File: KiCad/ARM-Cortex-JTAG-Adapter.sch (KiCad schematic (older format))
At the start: 5 parts, among them J1 Data, J2 Power

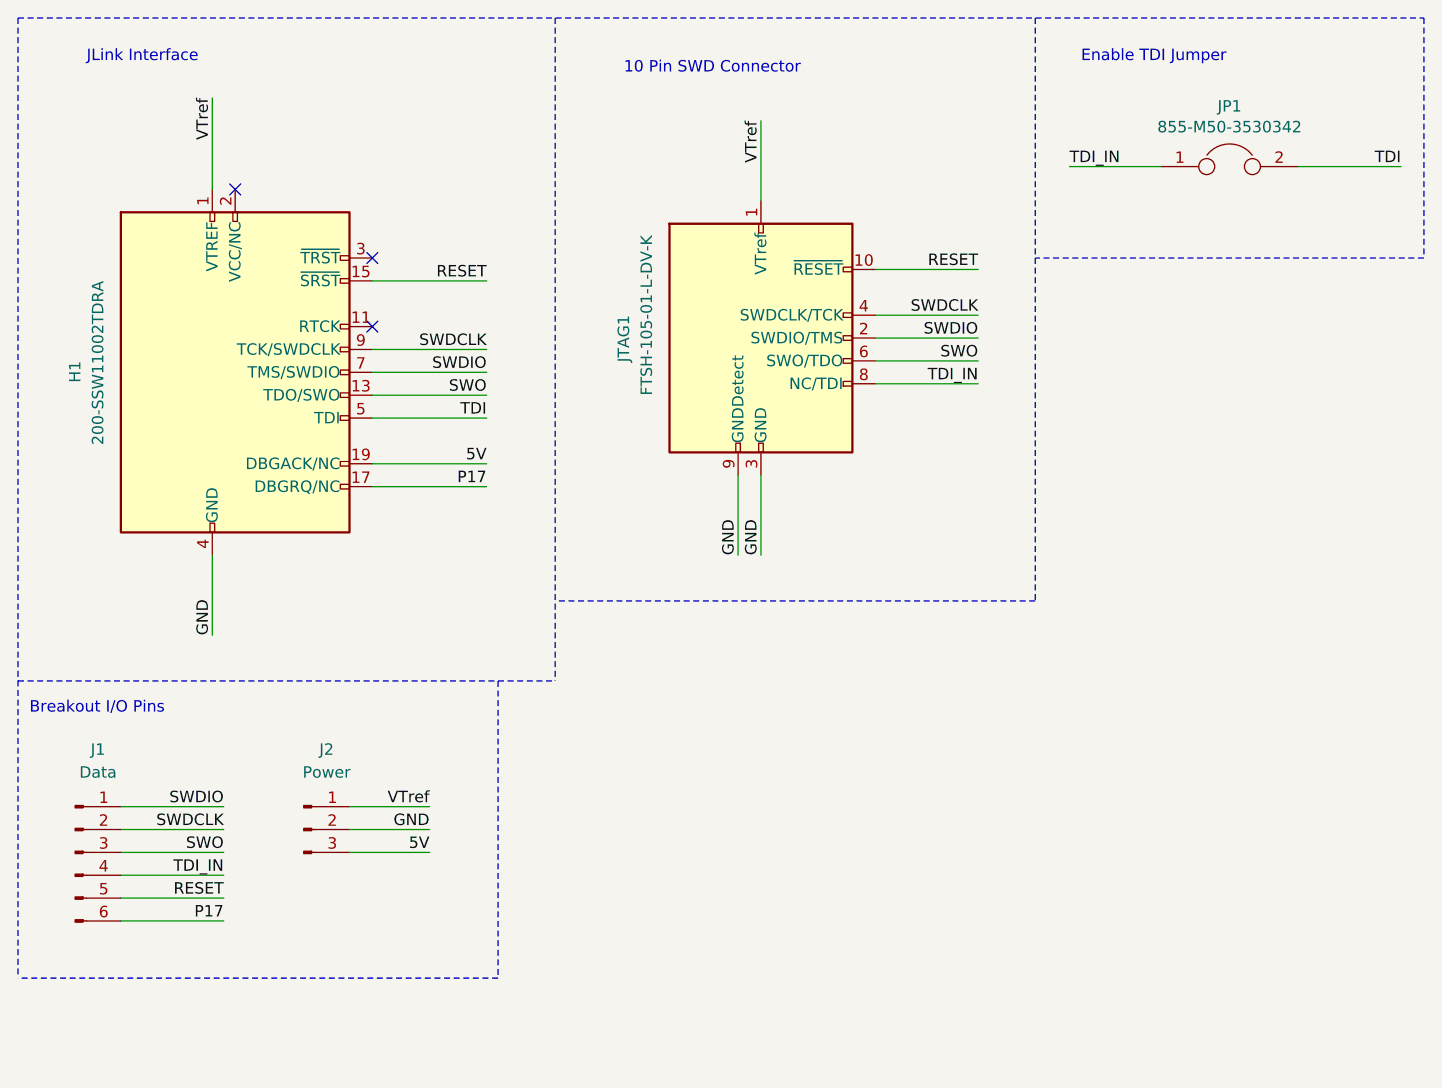
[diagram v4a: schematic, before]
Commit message: Redoing footprints and symbols.
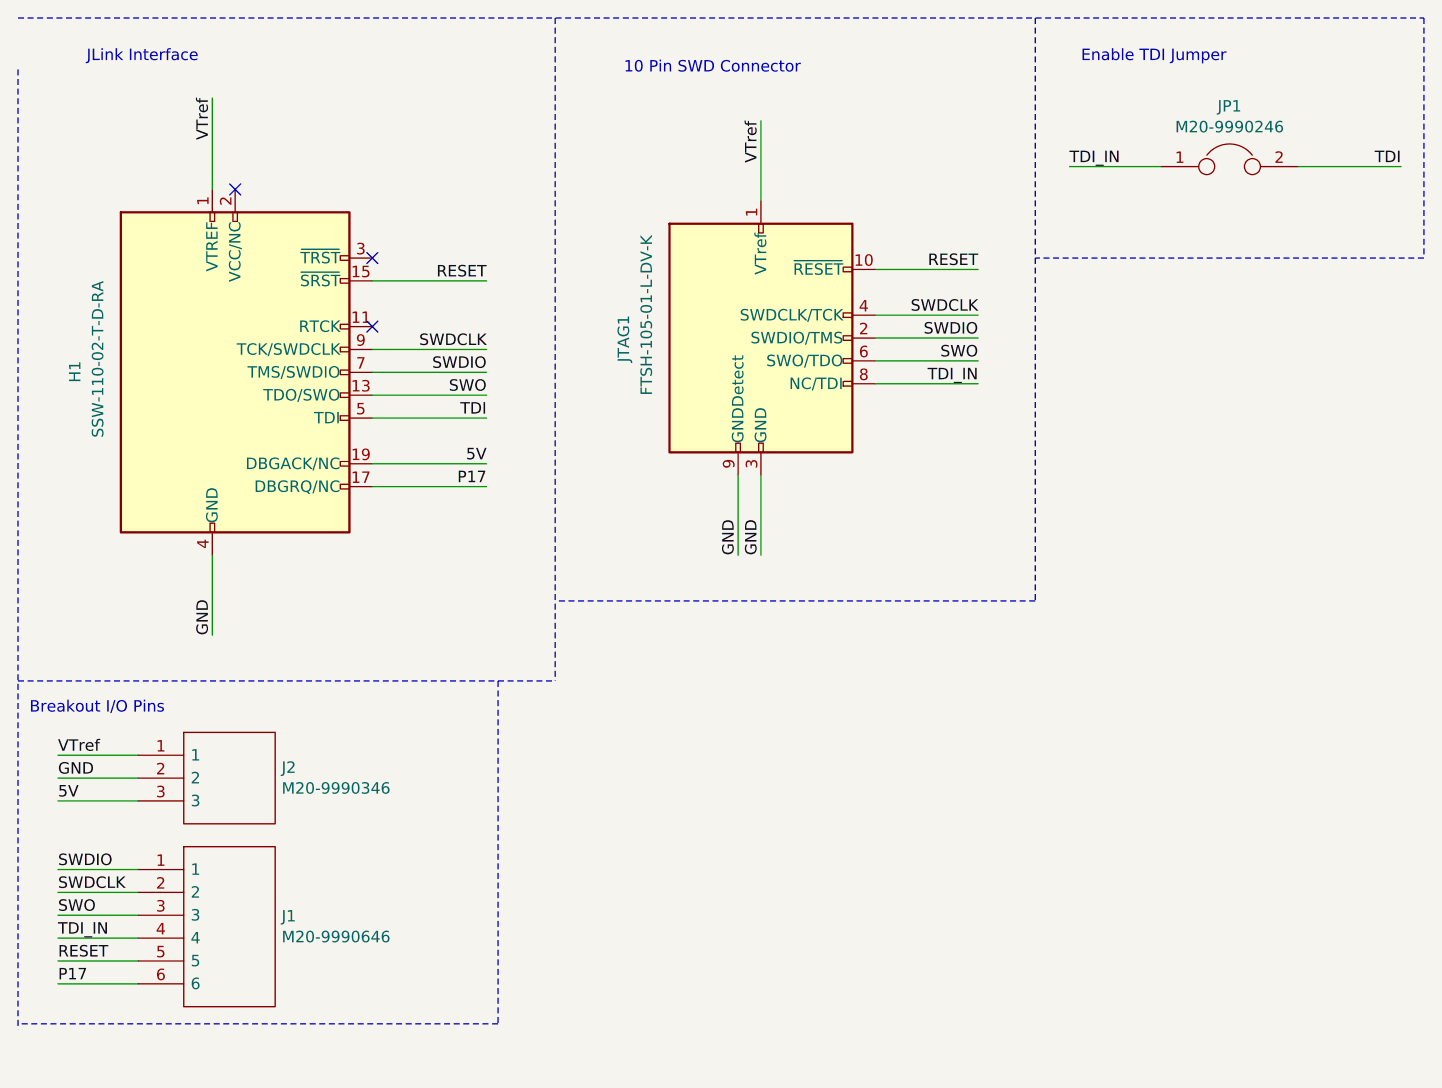
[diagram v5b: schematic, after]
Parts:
- removed J1: Data, Connector_PinHeader_2.54mm:PinHeader_1x06_P2.54mm_Vertical, symbol Connector:Conn_01x06_Male
- removed J2: Power, Connector_PinHeader_2.54mm:PinHeader_1x03_P2.54mm_Vertical, symbol Connector:Conn_01x03_Male
- added J1: M20-9990646, (Local):m20-9990646, symbol m20-9990646:M20-9990646
- added J2: M20-9990346, (Local):m20-9990346, symbol m20-9990346:M20-9990346
- H1: value 200-SSW11002TDRA -> SSW-110-02-T-D-RA
- JP1: value 855-M50-3530342 -> M20-9990246; footprint Connector_PinHeader_2.54mm:PinHeader_1x02_P2.54mm_Vertical -> (Local):M20-9990246
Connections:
- net 5V: now also J2.3
- net GND: now also J2.2
- net P17: now also J1.6
- net RESET: now also J1.5
- net SWDCLK: now also J1.2
- net SWDIO: now also J1.1
- net SWO: now also J1.3
- net TDI_IN: now also J1.4
- net VTref: now also J2.1
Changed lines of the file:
@@
 RESET
-$Comp
-L Connector:Conn_01x03_Male J2
-U 1 1 5F65A72D
-P 2450 4300
-F 0 "J2" H 2550 4650 50  0000 C CNN
-F 1 "Power" H 2550 4550 50  0000 C CNN
-F 2 "Connector_PinHeader_2.54mm:PinHeader_1x03_P2.54mm_Vertical" H 2450 4300 50  0001 C CNN
-F 3 "~" H 2450 4300 50  0001 C CNN
-	1    2450 4300
-	1    0    0    -1
-$EndComp
-Wire Wire Line
-	2650 4200 3000 4200
-Text Label 3000 4400 2    50   ~ 0
-5V
-Wire Wire Line
-	2650 4300 3000 4300
-Text Label 3000 4300 2    50   ~ 0
-GND
-Wire Wire Line
-	2650 4400 3000 4400
-Text Label 3000 4200 2    50   ~ 0
-VTref
-Wire Wire Line
-	1650 4200 2100 4200
-Text Label 2100 4300 2    50   ~ 0
-SWDCLK
-Wire Wire Line
-	1650 4300 2100 4300
-Text Label 2100 4200 2    50   ~ 0
-SWDIO
-Wire Wire Line
-	1650 4400 2100 4400
-Text Label 2100 4400 2    50   ~ 0
-SWO
-Wire Wire Line
-	1650 4500 2100 4500
-Text Label 2100 4500 2    50   ~ 0
-TDI_IN
 $Comp
 L Connector:Conn_ARM_JTAG_SWD_20 H1
@@
 P 2150 2300
 F 0 "H1" V 1450 2350 50  0000 R CNN
-F 1 "200-SSW11002TDRA" V 1550 2700 50  0000 R CNN
+F 1 "SSW-110-02-T-D-RA" V 1550 2700 50  0000 R CNN
 F 2 "Connector_IDC:IDC-Header_2x10_P2.54mm_Horizontal" H 2600 1250 50  0001 L TNN
 F 3 "http://infocenter.arm.com/help/topic/com.arm.doc.dui0499b/DUI0499B_system_design_reference.pdf" V 1800 1050 50  0001 C CNN
@@
 Text Label 3250 2800 2    50   ~ 0
 P17
-Wire Wire Line
-	1650 4600 2100 4600
-Text Label 2100 4600 2    50   ~ 0
-RESET
-Wire Wire Line
-	1650 4700 2100 4700
-Text Label 2100 4700 2    50   ~ 0
-P17
-$Comp
-L Connector:Conn_01x06_Male J1
-U 1 1 5F67F15F
-P 1450 4400
-F 0 "J1" H 1550 4850 50  0000 C CNN
-F 1 "Data" H 1550 4750 50  0000 C CNN
-F 2 "Connector_PinHeader_2.54mm:PinHeader_1x06_P2.54mm_Vertical" H 1450 4400 50  0001 C CNN
-F 3 "~" H 1450 4400 50  0001 C CNN
-	1    1450 4400
-	1    0    0    -1
-$EndComp
 Wire Notes Line
-	3300 3650 3300 4950
+	3300 3650 3300 5150
 Wire Notes Line
-	3300 4950 1200 4950
+	3300 5150 1200 5150
 Text Notes 1250 3800 0    50   ~ 0
 Breakout I/O Pins
@@
 	3550 750  3550 3650
 Wire Notes Line
-	1200 750  1200 4950
+	1200 975  1200 5175
 Wire Notes Line
 	1200 3650 3550 3650
@@
 P 6500 1400
 F 0 "JP1" H 6500 1664 50  0000 C CNN
-F 1 "855-M50-3530342" H 6500 1573 50  0000 C CNN
-F 2 "Connector_PinHeader_2.54mm:PinHeader_1x02_P2.54mm_Vertical" H 6500 1400 50  0001 C CNN
+F 1 "M20-9990246" H 6500 1573 50  0000 C CNN
+F 2 "(Local):M20-9990246" H 6500 1400 50  0001 C CNN
 F 3 "~" H 6500 1400 50  0001 C CNN
 	1    6500 1400
@@
 Text Label 5800 1400 0    50   ~ 0
 TDI_IN
+$Comp
+L m20-9990346:M20-9990346 J2
+U 1 1 5F867894
+P 1725 3975
+F 0 "J2" H 2353 3921 50  0000 L CNN
+F 1 "M20-9990346" H 2353 3830 50  0000 L CNN
+F 2 "(Local):m20-9990346" H 2375 4075 50  0001 L CNN
+F 3 "https://componentsearchengine.com/Datasheets/1/M20-9990346.pdf" H 2375 3975 50  0001 L CNN
+F 4 "03 SIL Vertical Pin Header HARWIN M20 Series, 2.54mm Pitch 3 Way 1 Row Straight PCB Header, Solder Termination, 3A" H 2375 3875 50  0001 L CNN "Description"
+F 5 "8.64" H 2375 3775 50  0001 L CNN "Height"
+F 6 "855-M20-9990346" H 2375 3675 50  0001 L CNN "Mouser Part Number"
+F 7 "https://www.mouser.com/Search/Refine.aspx?Keyword=855-M20-9990346" H 2375 3575 50  0001 L CNN "Mouser Price/Stock"
+F 8 "Harwin" H 2375 3475 50  0001 L CNN "Manufacturer_Name"
+F 9 "M20-9990346" H 2375 3375 50  0001 L CNN "Manufacturer_Part_Number"
+	1    1725 3975
+	1    0    0    -1
+$EndComp
+Wire Wire Line
+	1725 3975 1375 3975
+Wire Wire Line
+	1725 4075 1375 4075
+Text Label 1375 4075 0    50   ~ 0
+GND
+Text Label 1375 3975 0    50   ~ 0
+VTref
+Wire Wire Line
+	1725 4175 1375 4175
+Text Label 1375 4175 0    50   ~ 0
+5V
+$Comp
+L m20-9990646:M20-9990646 J1
+U 1 1 5F8664B1
+P 1725 4475
+F 0 "J1" H 2353 4271 50  0000 L CNN
+F 1 "M20-9990646" H 2353 4180 50  0000 L CNN
+F 2 "(Local):m20-9990646" H 2375 4575 50  0001 L CNN
+F 3 "https://componentsearchengine.com/Datasheets/2/M20-9990646.pdf" H 2375 4475 50  0001 L CNN
+F 4 "06 SIL Vertical Pin Header HARWIN M20 Series, 2.54mm Pitch 6 Way 1 Row Straight PCB Header, Solder Termination, 3A" H 2375 4375 50  0001 L CNN "Description"
+F 5 "8.64" H 2375 4275 50  0001 L CNN "Height"
+F 6 "855-M20-9990646" H 2375 4175 50  0001 L CNN "Mouser Part Number"
+F 7 "https://www.mouser.co.uk/ProductDetail/Harwin/M20-9990646?qs=Jph8NoUxIfXDcWZbabSSiw%3D%3D" H 2375 4075 50  0001 L CNN "Mouser Price/Stock"
+F 8 "Harwin" H 2375 3975 50  0001 L CNN "Manufacturer_Name"
+F 9 "M20-9990646" H 2375 3875 50  0001 L CNN "Manufacturer_Part_Number"
+	1    1725 4475
+	1    0    0    -1
+$EndComp
+Wire Wire Line
+	1725 4475 1375 4475
+Wire Wire Line
+	1725 4575 1375 4575
+Wire Wire Line
+	1725 4675 1375 4675
+Wire Wire Line
+	1725 4775 1375 4775
+Wire Wire Line
+	1725 4875 1375 4875
+Wire Wire Line
+	1725 4975 1375 4975
+Text Label 1375 4475 0    50   ~ 0
+SWDIO
+Text Label 1375 4575 0    50   ~ 0
+SWDCLK
+Text Label 1375 4675 0    50   ~ 0
+SWO
+Text Label 1375 4775 0    50   ~ 0
+TDI_IN
+Text Label 1375 4875 0    50   ~ 0
+RESET
+Text Label 1375 4975 0    50   ~ 0
+P17
 $EndSCHEMATC

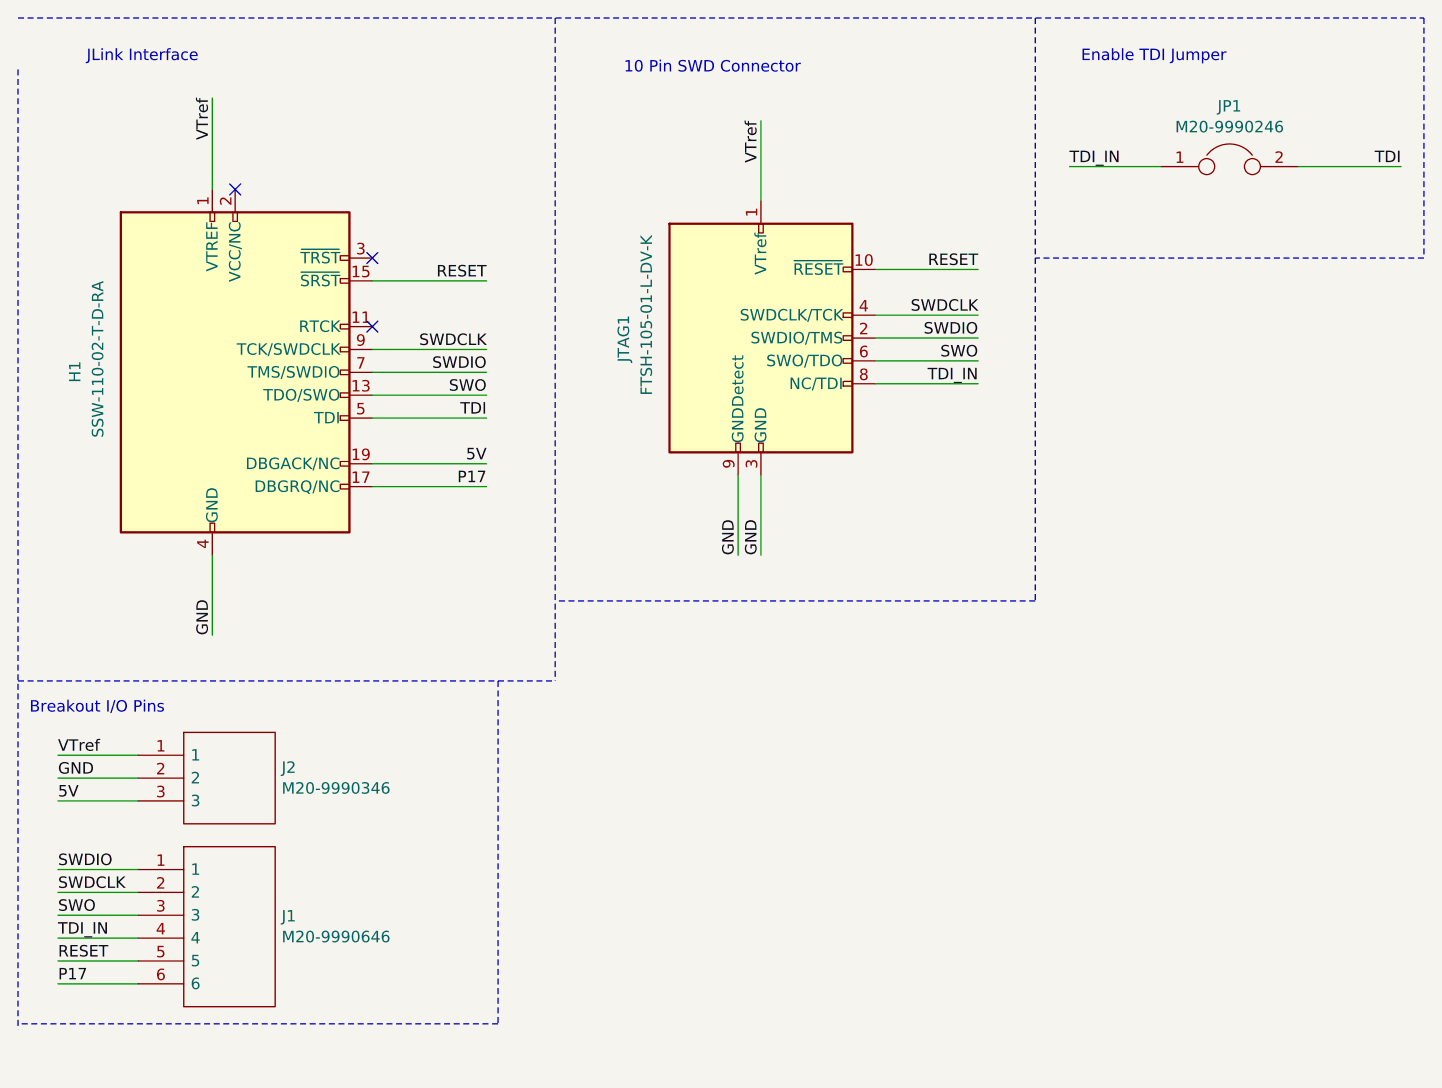
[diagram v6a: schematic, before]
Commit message: Adding Adafruit SWD connector module.
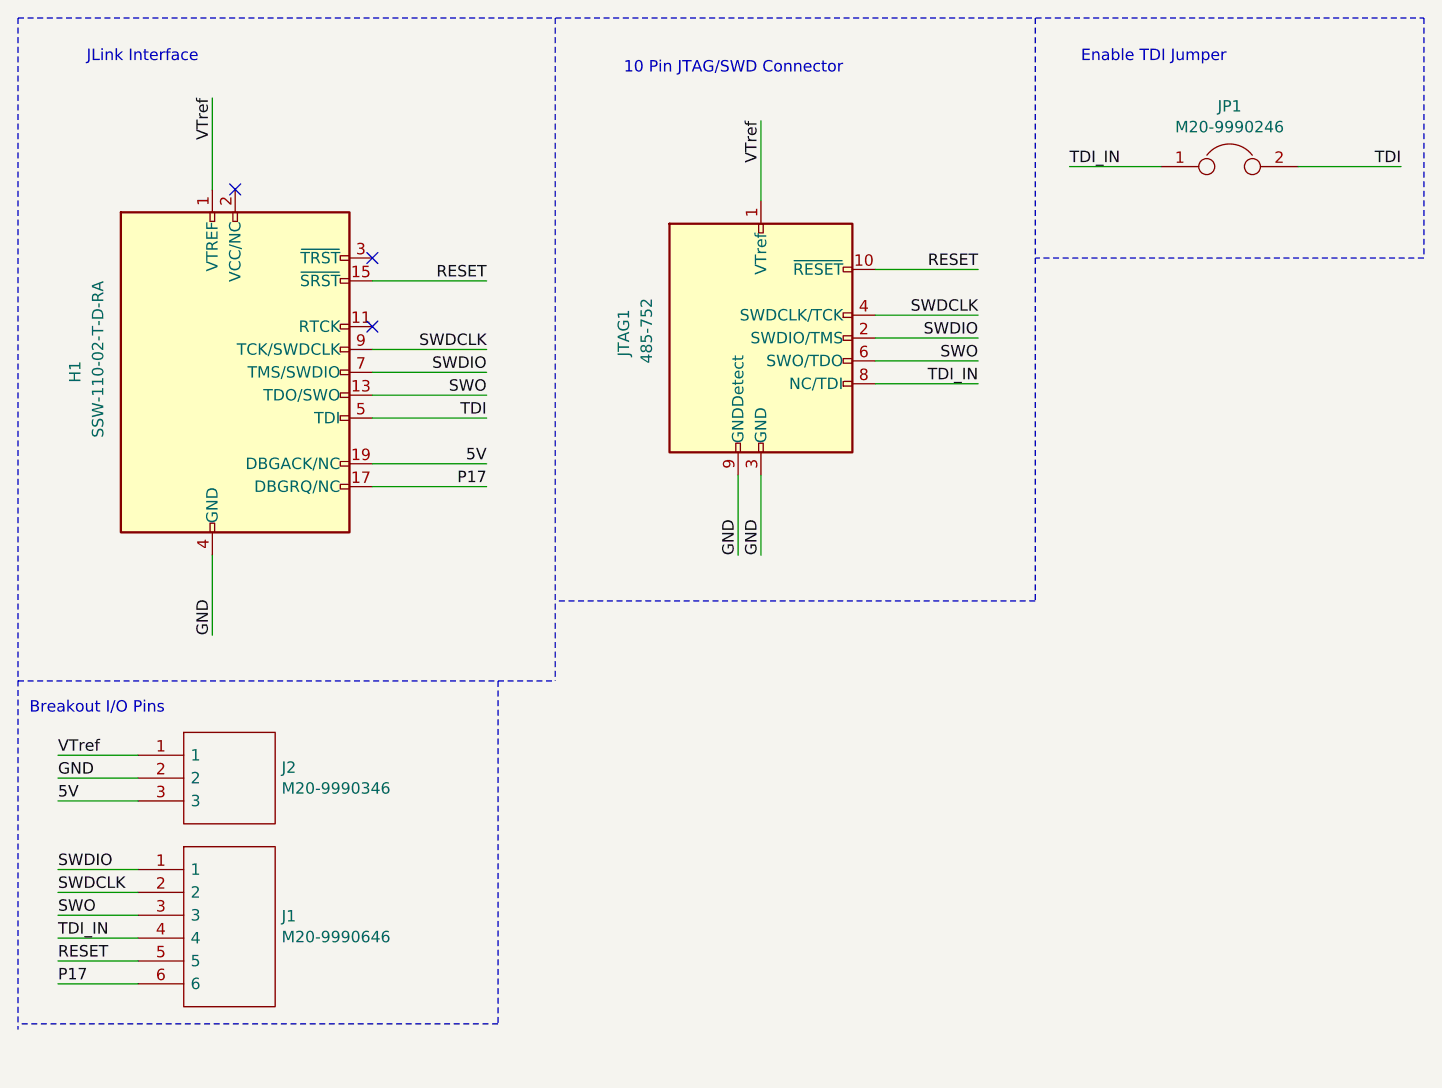
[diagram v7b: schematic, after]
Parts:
- JTAG1: value FTSH-105-01-L-DV-K -> 485-752; footprint (Local):SAMTEC-FTSH-105-01-X-DV -> (Local):Adafruit_SWD_Connector_PID_752; MPN (none) -> 458-752
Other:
- note added: "10 Pin JTAG/SWD Connector"
- note removed: "10 Pin SWD Connector"
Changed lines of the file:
@@
 U 1 1 5F64FD35
 P 4450 2150
-F 0 "JTAG1" V 3850 2250 50  0000 R CNN
-F 1 "FTSH-105-01-L-DV-K" V 3950 2600 50  0000 R CNN
-F 2 "(Local):SAMTEC-FTSH-105-01-X-DV" H 4450 2150 50  0001 C CNN
-F 3 "http://infocenter.arm.com/help/topic/com.arm.doc.ddi0314h/DDI0314H_coresight_components_trm.pdf" V 4100 900 50  0001 C CNN
+F 0 "JTAG1" V 3850 2275 50  0000 R CNN
+F 1 "485-752" V 3950 2325 50  0000 R CNN
+F 2 "(Local):Adafruit_SWD_Connector_PID_752" H 4450 2150 50  0001 C CNN
+F 3 "" V 4100 900 50  0001 C CNN
+F 4 "458-752" V 4450 2150 50  0001 C CNN "MPN"
 	1    4450 2150
 	1    0    0    -1
@@
 JLink Interface
 Text Notes 3850 1000 0    50   ~ 0
-10 Pin SWD Connector
+10 Pin JTAG/SWD Connector
 Wire Notes Line
 	5650 3300 3550 3300
@@
 	3550 750  3550 3650
 Wire Notes Line
-	1200 975  1200 5175
+	1200 750  1200 5175
 Wire Notes Line
 	1200 3650 3550 3650
